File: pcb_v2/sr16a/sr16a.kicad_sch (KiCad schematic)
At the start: 39 parts

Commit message: arquivos no note
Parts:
- removed D10, D11, D12: 1N4148, Diode_THT:D_DO-35_SOD27_P7.62mm_Horizontal, symbol Diode:1N4148
- removed D9: (no value), symbol Diode:1N4148
- removed R10, R9: (no value), symbol Device:R
- added C9: 100nF, Capacitor_THT:C_Disc_D5.1mm_W3.2mm_P5.00mm, symbol Device:C
- added U9: 74LS32, Package_DIP:DIP-14_W7.62mm, symbol 74xx:74LS32
- C1, C2, C3, C4, C5, C6, C7, C8: value (none) -> 100nF; footprint (none) -> Capacitor_THT:C_Disc_D5.1mm_W3.2mm_P5.00mm
- D1: value (none) -> LED; footprint (none) -> LED_THT:LED_D5.0mm
- D2, D3, D4, D5, D6, D7, D8: footprint (none) -> LED_THT:LED_D5.0mm
- J1: value (none) -> Conn_02x22_Top_Bottom; footprint (none) -> edge_connector:edge-connector-44
- R1, R2, R3, R4, R5, R6, R7, R8: value (none) -> 1K; footprint (none) -> Resistor_THT:R_Axial_DIN0207_L6.3mm_D2.5mm_P7.62mm_Horizontal
- U1, U2, U3, U4: value (none) -> 74LS193; footprint (none) -> Package_DIP:DIP-16_W7.62mm
- U5, U6, U7, U8: value (none) -> 74LS244; footprint (none) -> Package_DIP:DIP-20_W7.62mm
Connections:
- net +5V: now also C9.2, U9.14 (VCC)
- net GND: now also C9.1, U9.10, U9.12, U9.13, U9.7 (GND), U9.9
- net count_down: now also U9.5
- net count_up: now also U9.2
- net dec: now also U9.6
- net inc: now also U9.3
- net ~{clock}: now also U9.1, U9.4
- no-connect marks 10 -> 12

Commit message: arquivos do gdrive
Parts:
- removed C9: 100nF, Capacitor_THT:C_Disc_D5.1mm_W3.2mm_P5.00mm, symbol Device:C
- removed U9: 74LS32, Package_DIP:DIP-14_W7.62mm, symbol 74xx:74LS32
- added D10, D11, D12, D9: 1N4148, Diode_THT:D_DO-35_SOD27_P7.62mm_Horizontal, symbol Diode:1N4148
- added R10, R9: 10K, Resistor_THT:R_Axial_DIN0207_L6.3mm_D2.5mm_P7.62mm_Horizontal, symbol Device:R
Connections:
- net GND: now also R10.2, R9.2
- net count_down: now also D12.2 (A)
- net count_up: now also D10.2 (A)
- net dec: now also D11.1 (K), D12.1 (K), R10.1
- net inc: now also D10.1 (K), D9.1 (K), R9.1
- net ~{clock}: now also D11.2 (A), D9.2 (A)
- no-connect marks 12 -> 10

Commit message: adicionados o designador e o swap para a arquivo reg16
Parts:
- removed D10, D11, D12, D9: 1N4148, Diode_THT:D_DO-35_SOD27_P7.62mm_Horizontal, symbol Diode:1N4148
- removed R10, R9: 10K, Resistor_THT:R_Axial_DIN0207_L6.3mm_D2.5mm_P7.62mm_Horizontal, symbol Device:R
- added C9: 100nF, Capacitor_SMD:C_1206_3216Metric_Pad1.33x1.80mm_HandSolder, symbol Device:C
- added U9: 74LS32, Package_DIP:SMDIP-14_W7.62mm, symbol 74xx:74LS32
- C1, C2, C3, C4, C5, C6, C7, C8: footprint Capacitor_THT:C_Disc_D5.1mm_W3.2mm_P5.00mm -> Capacitor_SMD:C_1206_3216Metric_Pad1.33x1.80mm_HandSolder
- R1, R2, R3, R4, R5, R6, R7, R8: footprint Resistor_THT:R_Axial_DIN0207_L6.3mm_D2.5mm_P7.62mm_Horizontal -> Resistor_SMD:R_1206_3216Metric_Pad1.30x1.75mm_HandSolder
- U1, U2, U3, U4: footprint Package_DIP:DIP-16_W7.62mm -> Package_DIP:SMDIP-16_W7.62mm
- U5, U6, U7, U8: footprint Package_DIP:DIP-20_W7.62mm -> Package_DIP:SMDIP-20_W7.62mm
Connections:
- net +5V: now also C9.2, U9.14 (VCC)
- net GND: now also C9.1, U9.10, U9.12, U9.13, U9.7 (GND), U9.9
- net count_down: now also U9.5
- net count_up: now also U9.2
- net dec: now also U9.6
- net inc: now also U9.3
- net ~{clock}: now also U9.1, U9.4
- no-connect marks 10 -> 12

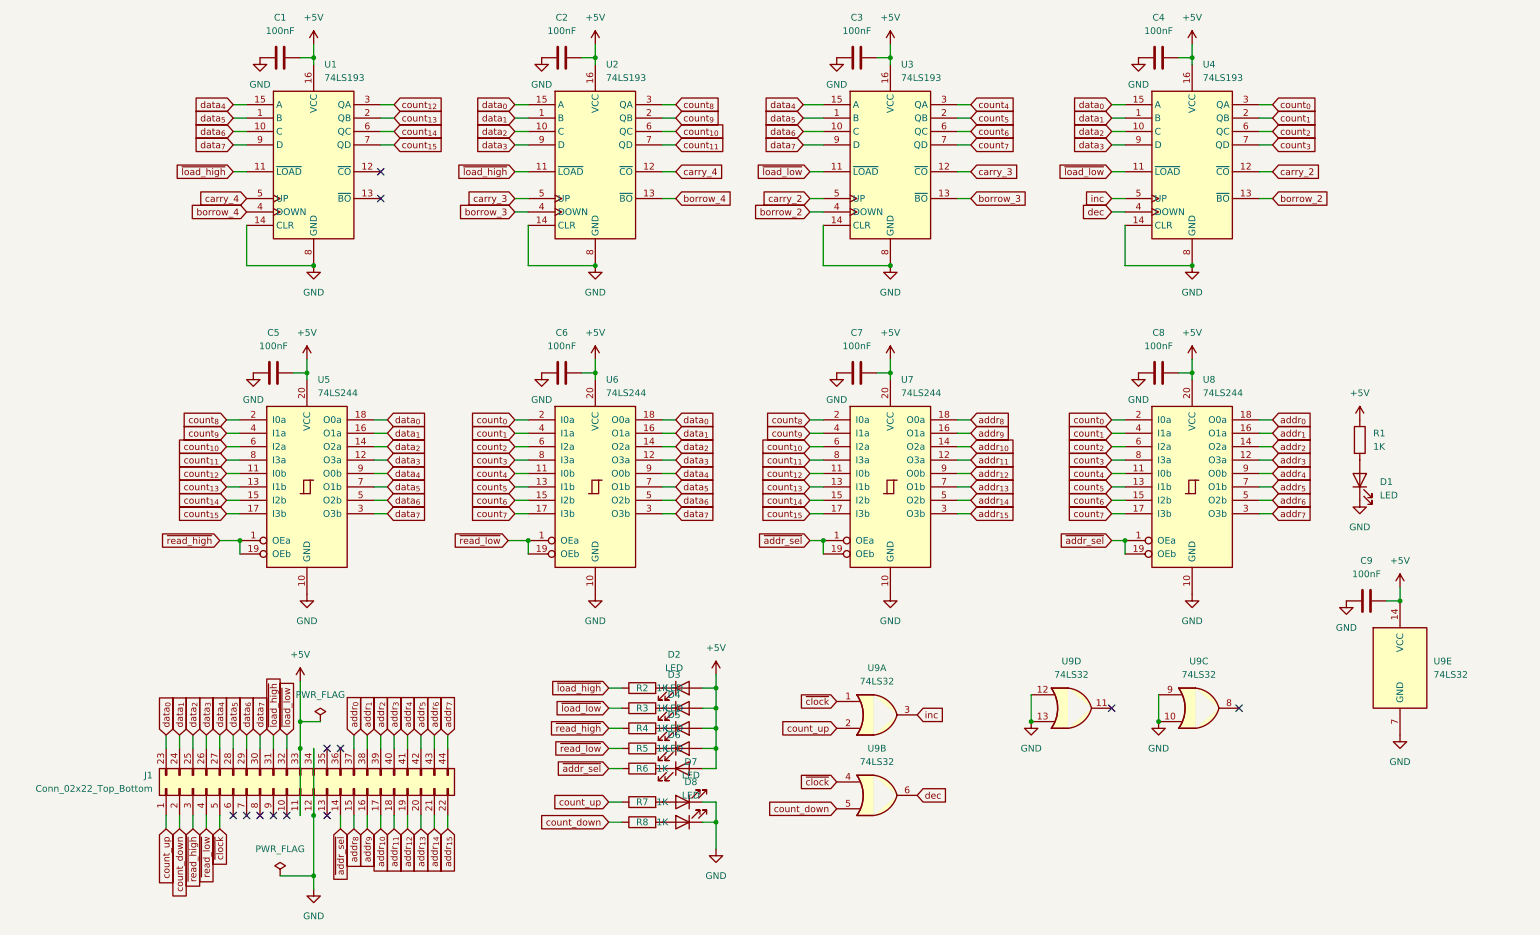
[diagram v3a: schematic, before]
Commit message: concluido o desenho das placas satelite do banco de registradores de 16 bits
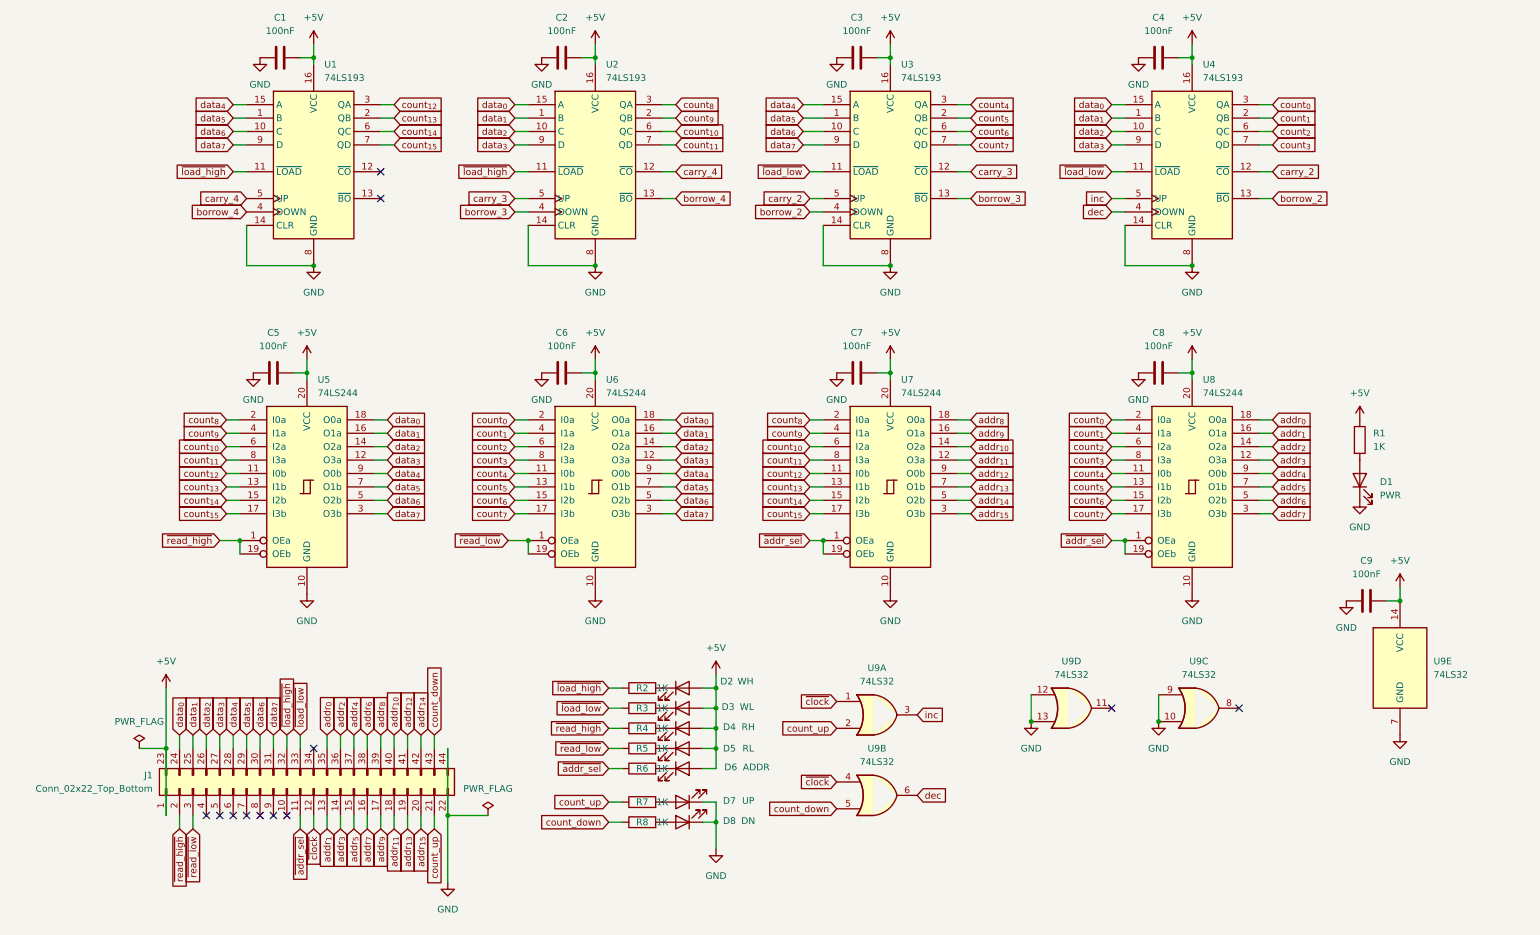
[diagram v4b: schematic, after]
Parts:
- C1, C2, C3, C4, C5, C6, C7, C8, C9: footprint Capacitor_SMD:C_1206_3216Metric_Pad1.33x1.80mm_HandSolder -> Capacitor_THT:C_Disc_D5.1mm_W3.2mm_P5.00mm
- D1: value LED -> PWR
- D2: value LED -> WH
- D3: value LED -> WL
- D4: value LED -> RH
- D5: value LED -> RL
- D6: value LED -> ADDR
- D7: value LED -> UP
- D8: value LED -> DN
- R1, R2, R3, R4, R5, R6, R7, R8: footprint Resistor_SMD:R_1206_3216Metric_Pad1.30x1.75mm_HandSolder -> Resistor_THT:R_Axial_DIN0204_L3.6mm_D1.6mm_P7.62mm_Horizontal
- U1, U2, U3, U4: footprint Package_DIP:SMDIP-16_W7.62mm -> Package_DIP:DIP-16_W7.62mm
- U5, U6, U7, U8: footprint Package_DIP:SMDIP-20_W7.62mm -> Package_DIP:DIP-20_W7.62mm
- U9: footprint Package_DIP:SMDIP-14_W7.62mm -> Package_DIP:DIP-14_W7.62mm
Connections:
- net +5V: now also J1.1 (Pin_1), J1.23 (Pin_23); no longer J1.11 (Pin_11), J1.33 (Pin_33)
- net GND: now also J1.22 (Pin_22), J1.44 (Pin_44); no longer J1.12 (Pin_12), J1.34 (Pin_34)
- net addr_{0}: now also J1.35 (Pin_35); no longer J1.37 (Pin_37)
- net addr_{10}: now also J1.40 (Pin_40); no longer J1.17 (Pin_17)
- net addr_{12}: now also J1.41 (Pin_41); no longer J1.19 (Pin_19)
- net addr_{13}: now also J1.19 (Pin_19); no longer J1.20 (Pin_20)
- net addr_{14}: now also J1.42 (Pin_42); no longer J1.21 (Pin_21)
- net addr_{15}: now also J1.20 (Pin_20); no longer J1.22 (Pin_22)
- net addr_{1}: now also J1.13 (Pin_13); no longer J1.38 (Pin_38)
- net addr_{2}: now also J1.36 (Pin_36); no longer J1.39 (Pin_39)
- net addr_{3}: now also J1.14 (Pin_14); no longer J1.40 (Pin_40)
- net addr_{4}: now also J1.37 (Pin_37); no longer J1.41 (Pin_41)
- net addr_{5}: now also J1.15 (Pin_15); no longer J1.42 (Pin_42)
- net addr_{6}: now also J1.38 (Pin_38); no longer J1.43 (Pin_43)
- net addr_{7}: now also J1.16 (Pin_16); no longer J1.44 (Pin_44)
- net addr_{8}: now also J1.39 (Pin_39); no longer J1.15 (Pin_15)
- net addr_{9}: now also J1.17 (Pin_17); no longer J1.16 (Pin_16)
- net count_down: now also J1.43 (Pin_43); no longer J1.2 (Pin_2)
- net count_up: now also J1.21 (Pin_21); no longer J1.1 (Pin_1)
- net data_{0}: now also J1.24 (Pin_24); no longer J1.23 (Pin_23)
- net data_{1}: now also J1.25 (Pin_25); no longer J1.24 (Pin_24)
- net data_{2}: now also J1.26 (Pin_26); no longer J1.25 (Pin_25)
- net data_{3}: now also J1.27 (Pin_27); no longer J1.26 (Pin_26)
- net data_{4}: now also J1.28 (Pin_28); no longer J1.27 (Pin_27)
- net data_{5}: now also J1.29 (Pin_29); no longer J1.28 (Pin_28)
- net data_{6}: now also J1.30 (Pin_30); no longer J1.29 (Pin_29)
- net data_{7}: now also J1.31 (Pin_31); no longer J1.30 (Pin_30)
- net ~{addr_sel}: now also J1.11 (Pin_11); no longer J1.14 (Pin_14)
- net ~{clock}: now also J1.12 (Pin_12); no longer J1.5 (Pin_5)
- net ~{load_high}: now also J1.32 (Pin_32); no longer J1.31 (Pin_31)
- net ~{load_low}: now also J1.33 (Pin_33); no longer J1.32 (Pin_32)
- net ~{read_high}: now also J1.2 (Pin_2); no longer J1.3 (Pin_3)
- net ~{read_low}: now also J1.3 (Pin_3); no longer J1.4 (Pin_4)
